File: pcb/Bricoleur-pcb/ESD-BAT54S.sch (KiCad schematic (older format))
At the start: 1 part

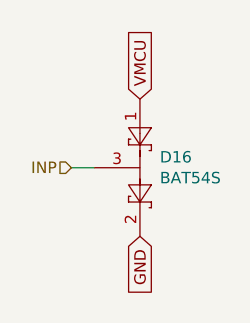
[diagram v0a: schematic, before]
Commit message: Power and clock networks ready (probably).
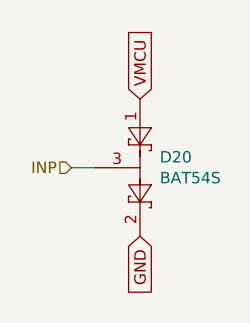
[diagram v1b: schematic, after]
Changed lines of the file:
@@
 AR Path="/5BEE7FFD/5BEC0258/5BB71F8A" Ref="D19"  Part="1"
 AR Path="/5BEE7FFD/5BEC025B/5BB71F8A" Ref="D20"  Part="1"
-F 0 "D16" V 5804 3037 50  0000 L CNN
+F 0 "D20" V 5804 3037 50  0000 L CNN
 F 1 "BAT54S" V 5895 3037 50  0000 L CNN
 F 2 "Package_TO_SOT_SMD:SOT-23" H 5925 3075 50  0001 L CNN

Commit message: Moar routing
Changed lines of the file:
@@
 AR Path="/5BEE7FFD/5BEC0258/5BB71F8A" Ref="D19"  Part="1"
 AR Path="/5BEE7FFD/5BEC025B/5BB71F8A" Ref="D20"  Part="1"
-F 0 "D20" V 5804 3037 50  0000 L CNN
+F 0 "D16" V 5804 3037 50  0000 L CNN
 F 1 "BAT54S" V 5895 3037 50  0000 L CNN
 F 2 "Package_TO_SOT_SMD:SOT-23" H 5925 3075 50  0001 L CNN
